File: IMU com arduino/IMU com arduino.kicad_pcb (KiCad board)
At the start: 2 copper layers, 2 parts, among them J1 IMU

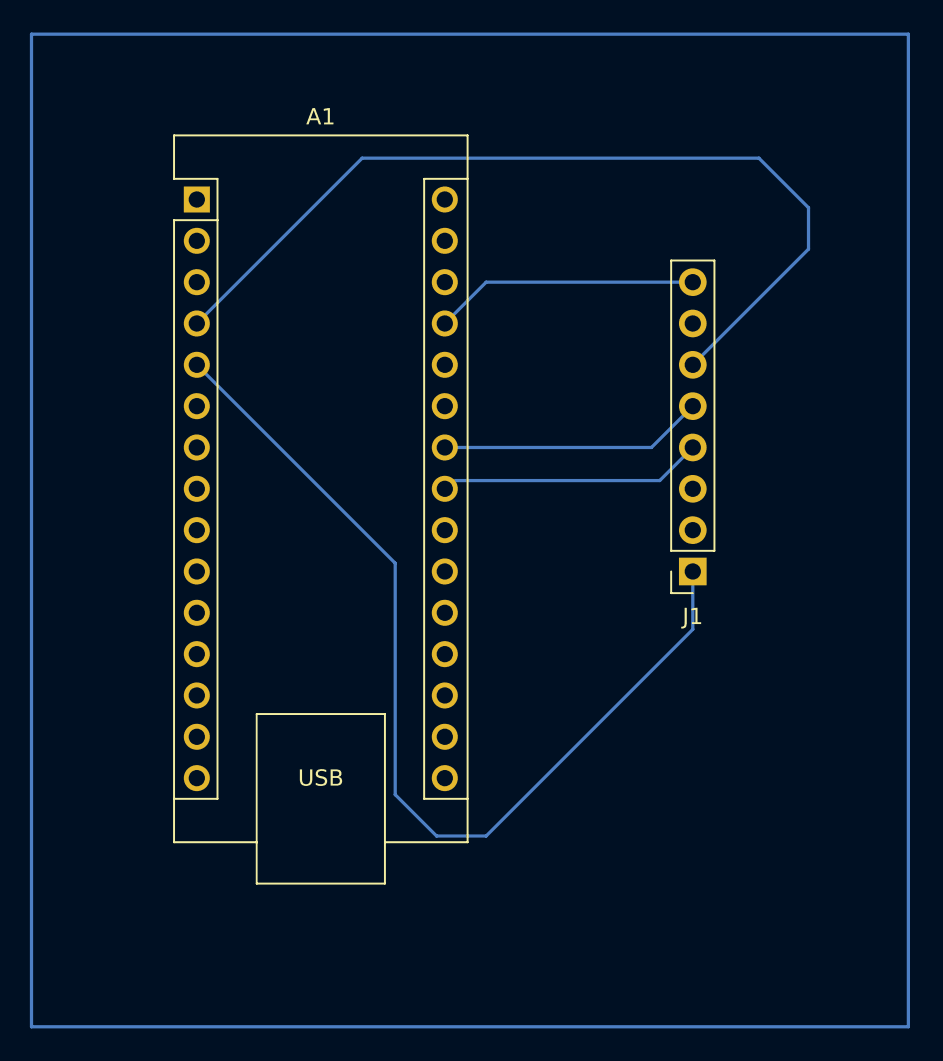
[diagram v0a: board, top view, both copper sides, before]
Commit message: primeiro protótipo da placa integrada (comunicação e potencia)
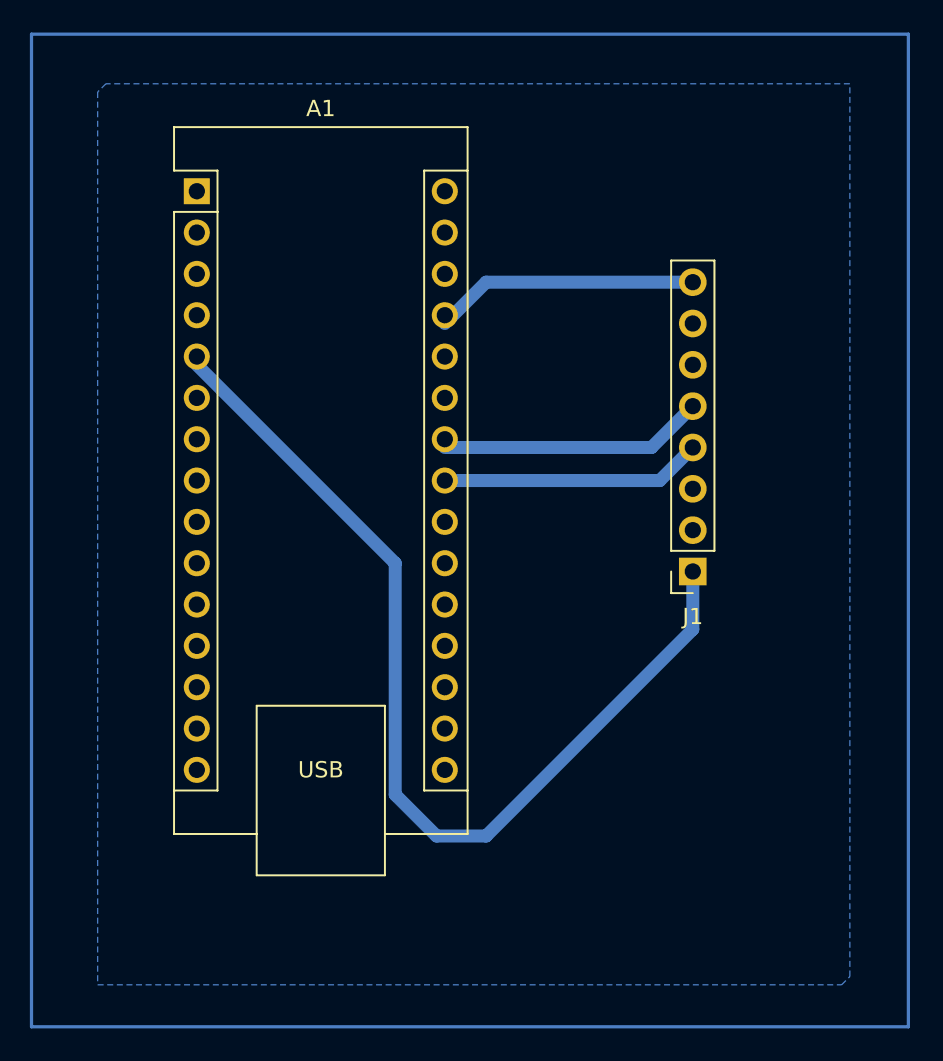
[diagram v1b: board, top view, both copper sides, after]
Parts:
- moved A1 0.51 mm to (66.0, 24.9)
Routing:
- net GND: track 55.7 -> 0.00 mm
- added copper zone on B.Cu, net GND
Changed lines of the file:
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@@
 			(outputformat 1)
 			(mirror no)
-			(drillshape 1)
+			(drillshape 0)
 			(scaleselection 1)
-			(outputdirectory "")
+			(outputdirectory "./")
 		)
 	)
@@
 	(footprint "Module:Arduino_Nano"
 		(layer "F.Cu")
-		(at 66.04 25.4)
+		(at 66.04 24.892)
 		(descr "Arduino Nano, http://www.mouser.com/pdfdocs/Gravitech_Arduino_Nano3_0.pdf")
 		(tags "Arduino Nano")
@@
 		(start 83.82 30.48)
 		(end 81.28 33.02)
-		(width 0.2)
+		(width 0.8)
 		(layer "B.Cu")
 		(net 3)
@@
 		(start 96.52 30.48)
 		(end 83.82 30.48)
-		(width 0.2)
+		(width 0.8)
 		(layer "B.Cu")
 		(net 3)
@@
 		(start 93.98 40.64)
 		(end 81.28 40.64)
-		(width 0.2)
+		(width 0.8)
 		(layer "B.Cu")
 		(net 7)
@@
 		(start 96.52 38.1)
 		(end 93.98 40.64)
-		(width 0.2)
+		(width 0.8)
 		(layer "B.Cu")
 		(net 7)
@@
 		(start 94.488 42.672)
 		(end 81.788 42.672)
-		(width 0.2)
+		(width 0.8)
 		(layer "B.Cu")
 		(net 9)
@@
 		(start 96.52 40.64)
 		(end 94.488 42.672)
-		(width 0.2)
+		(width 0.8)
 		(layer "B.Cu")
 		(net 9)
@@
 		(start 83.82 64.516)
 		(end 96.52 51.816)
-		(width 0.2)
+		(width 0.8)
 		(layer "B.Cu")
 		(net 21)
@@
 		(start 80.772 64.516)
 		(end 83.82 64.516)
-		(width 0.2)
+		(width 0.8)
 		(layer "B.Cu")
 		(net 21)
@@
 		(start 78.232 47.752)
 		(end 78.232 61.976)
-		(width 0.2)
+		(width 0.8)
 		(layer "B.Cu")
 		(net 21)
@@
 		(start 78.232 61.976)
 		(end 80.772 64.516)
-		(width 0.2)
+		(width 0.8)
 		(layer "B.Cu")
 		(net 21)
@@
 		(start 66.04 35.56)
 		(end 78.232 47.752)
-		(width 0.2)
+		(width 0.8)
 		(layer "B.Cu")
 		(net 21)
@@
 		(start 96.52 51.816)
 		(end 96.52 48.26)
-		(width 0.2)
+		(width 0.8)
 		(layer "B.Cu")
 		(net 21)
 	)
-	(segment
-		(start 103.632 25.908)
-		(end 100.584 22.86)
-		(width 0.2)
-		(layer "B.Cu")
+	(zone
 		(net 33)
-	)
-	(segment
-		(start 96.52 35.56)
-		(end 103.632 28.448)
-		(width 0.2)
-		(layer "B.Cu")
-		(net 33)
-	)
-	(segment
-		(start 66.04 33.02)
-		(end 76.2 22.86)
-		(width 0.2)
-		(layer "B.Cu")
-		(net 33)
-	)
-	(segment
-		(start 100.584 22.86)
-		(end 76.2 22.86)
-		(width 0.2)
-		(layer "B.Cu")
-		(net 33)
-	)
-	(segment
-		(start 103.632 28.448)
-		(end 103.632 25.908)
-		(width 0.2)
-		(layer "B.Cu")
-		(net 33)
+		(net_name "GND")
+		(layer "B.Cu")
+		(hatch edge 0.5)
+		(connect_pads
+			(clearance 0.75)
+		)
+		(min_thickness 0.25)
+		(filled_areas_thickness no)
+		(fill yes
+			(thermal_gap 0.5)
+			(thermal_bridge_width 0.5)
+		)
+		(polygon
+			(pts
+				(xy 59.944 18.796) (xy 59.944 73.66) (xy 105.664 73.66) (xy 106.172 73.152) (xy 106.172 18.288)
+				(xy 60.452 18.288)
+			)
+		)
 	)
 )

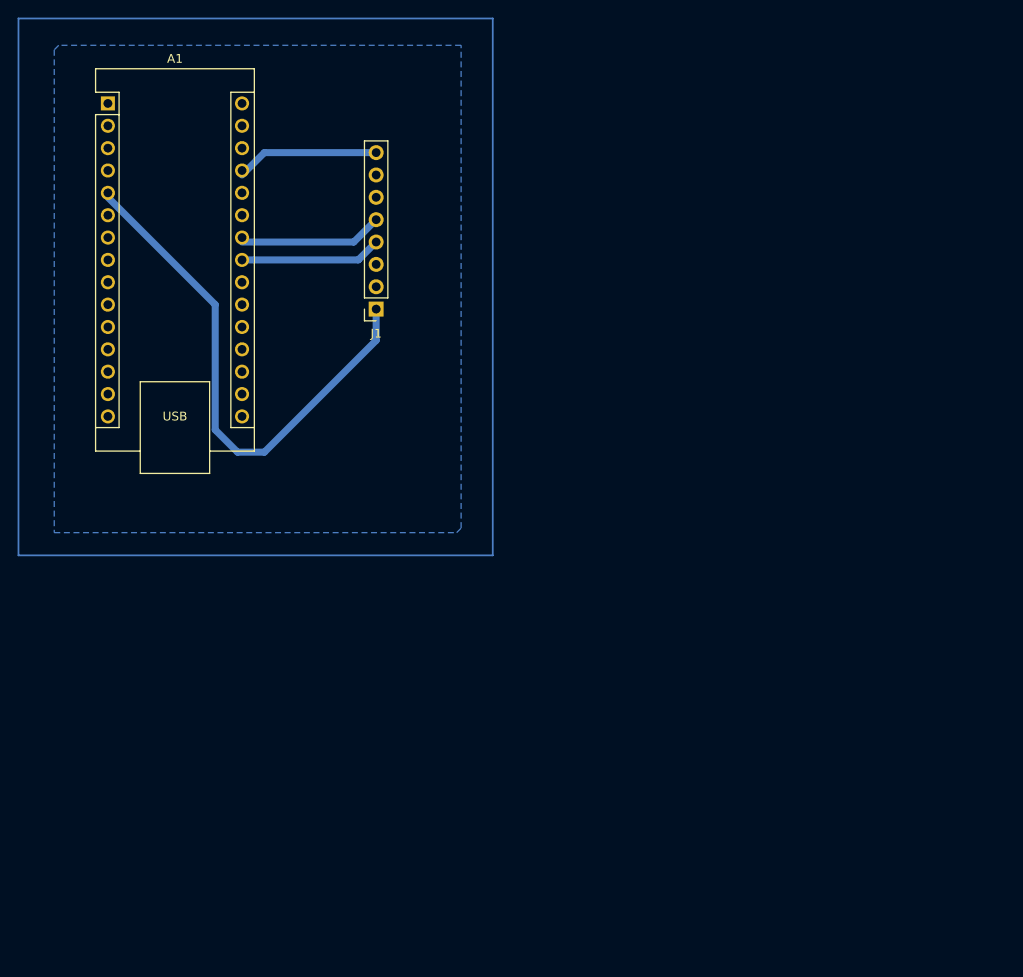
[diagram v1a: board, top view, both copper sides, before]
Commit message: imu nova (MPU6050)
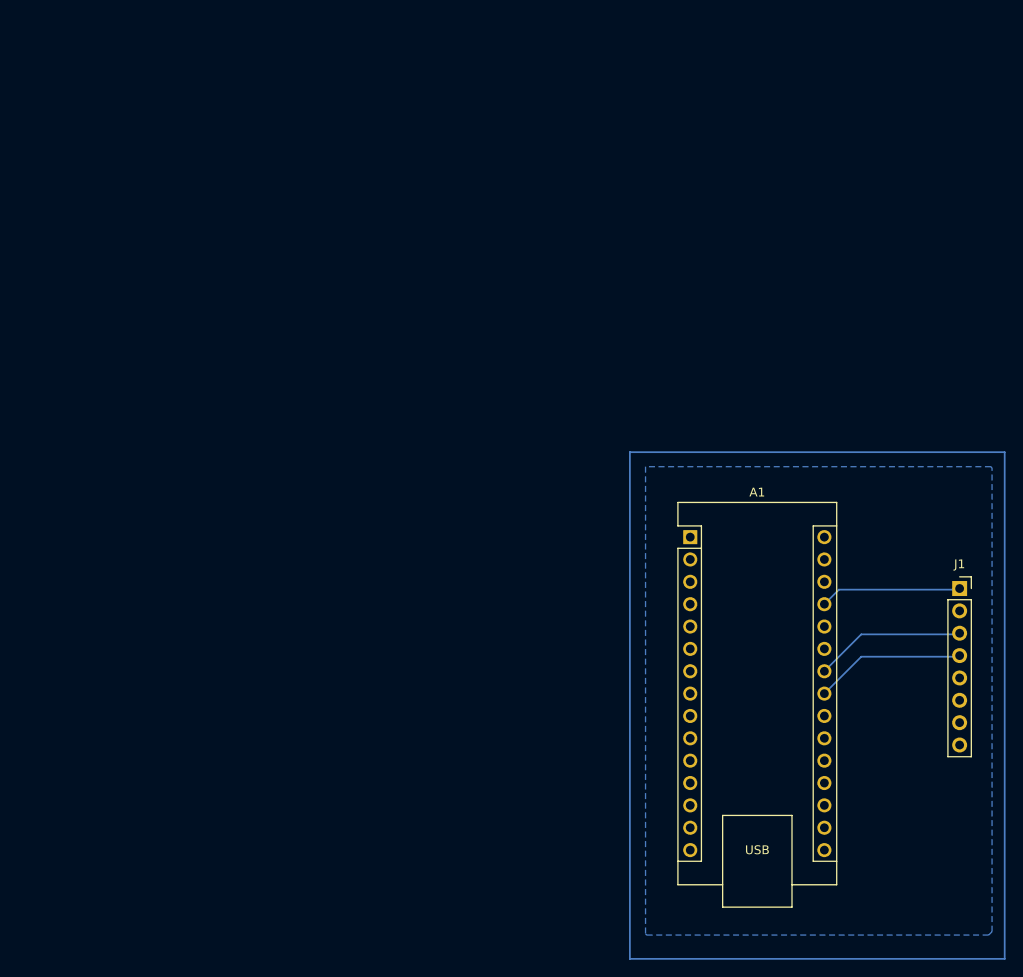
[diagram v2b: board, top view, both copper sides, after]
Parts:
- moved A1 82.5 mm to (132.2, 74.2)
- moved J1 73.5 mm to (162.8, 80.0), turned to 0 degrees
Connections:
- A1 pad 5: Net-(A1-D2) -> unconnected-(A1-D2-Pad5)
- J1 pad 1: Net-(A1-D2) -> Net-(A1-+5V)
- J1 pad 2: unconnected-(J1-Pin_2-Pad2) -> GND
- J1 pad 3: unconnected-(J1-Pin_3-Pad3) -> Net-(A1-A5)
- J1 pad 5: Net-(A1-A5) -> unconnected-(J1-Pin_5-Pad5)
- J1 pad 6: GND -> unconnected-(J1-Pin_6-Pad6)
- J1 pad 8: Net-(A1-+5V) -> unconnected-(J1-Pin_8-Pad8)
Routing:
- net Net-(A1-D2): track 59.6 -> 0.00 mm
- net Net-(A1-A4): track 16.3 -> 17.8 mm
- net Net-(A1-A5): track 16.3 -> 17.1 mm
